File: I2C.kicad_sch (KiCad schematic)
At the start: 16 parts, among them J701 Conn_01x04, J702 Conn_01x04

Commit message: HALMET redesign
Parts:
- removed J701: Conn_01x04, Connector_JST:JST_SH_BM04B-SRSS-TB_1x04-1MP_P1.00mm_Vertical, symbol Connector_Generic:Conn_01x04
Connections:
- net SCL_CONN: now also J702.4 (Pin_4); no longer J702.3 (Pin_3)
- net SDA_CONN: now also J702.3 (Pin_3); no longer J702.4 (Pin_4)
- net +3V3 renamed +3.3V
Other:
- note removed: "I2C (qwiic)"
- title: Sailor Hat with ESP32 -> Hat Labs Marine Engine/Tank interface (HALMET)

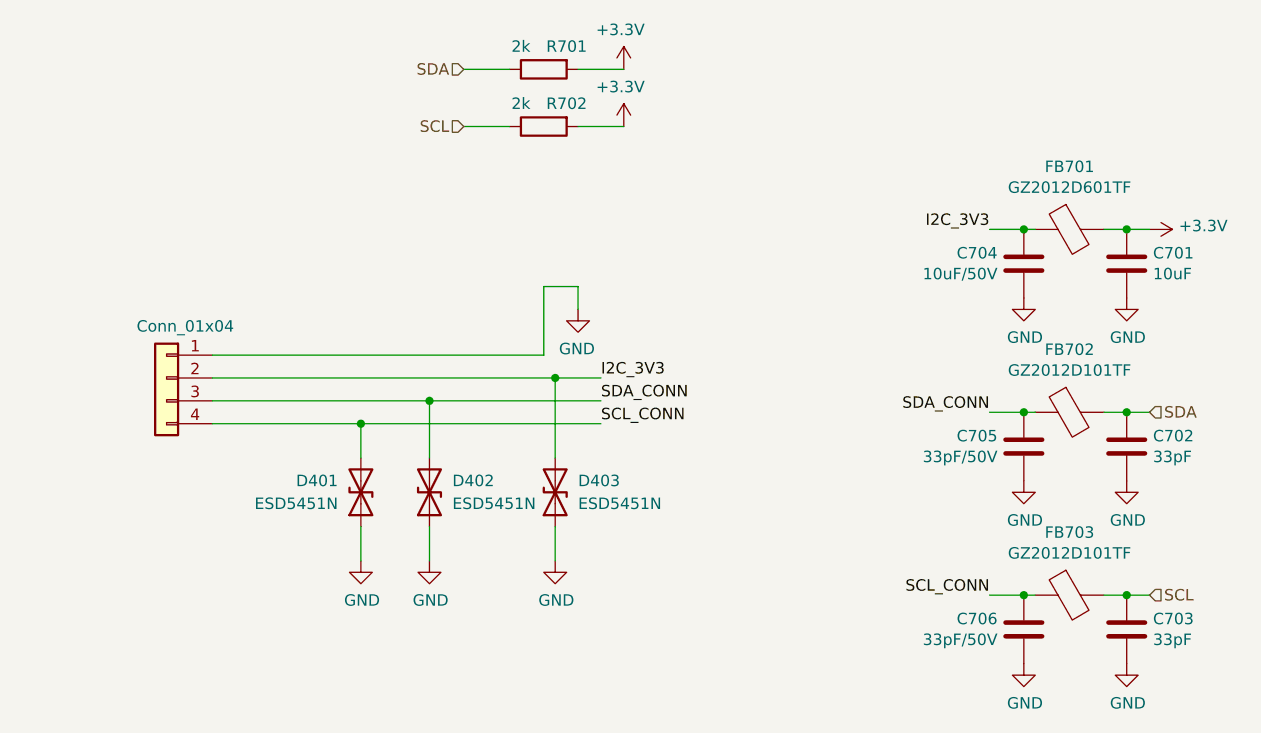
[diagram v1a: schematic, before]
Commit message: Implement HALMET v1.0.0 design changes
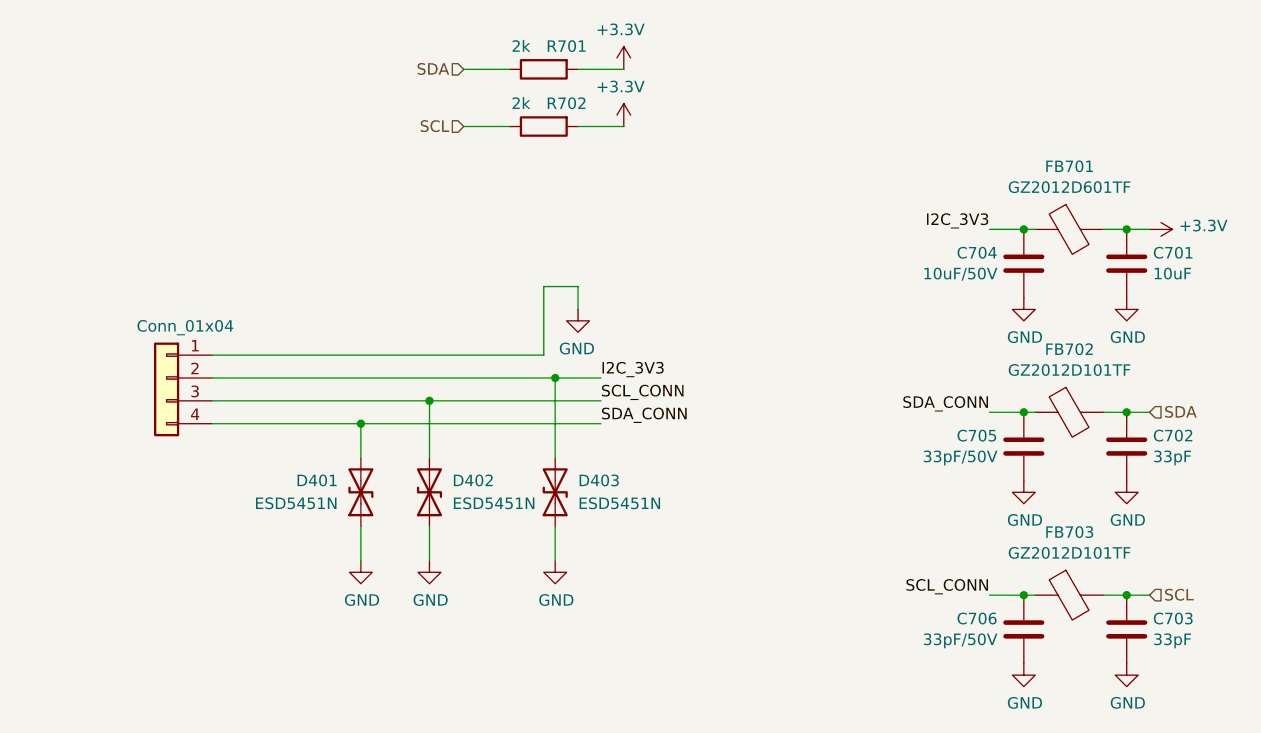
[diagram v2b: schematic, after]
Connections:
- net SCL_CONN: now also D402.2 (A2), J702.3 (Pin_3); no longer D401.2 (A2), J702.4 (Pin_4)
- net SDA_CONN: now also D401.2 (A2), J702.4 (Pin_4); no longer D402.2 (A2), J702.3 (Pin_3)
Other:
- title: Hat Labs Marine Engine/Tank interface (HALMET) -> Hat Labs Marine Engine & Tank interface (HALMET)
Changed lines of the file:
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@@
   (paper "A4")
   (title_block
-    (title "Hat Labs Marine Engine/Tank interface (HALMET)")
-    (date "2023-09-19")
-    (rev "1.0.0-a1")
+    (title "Hat Labs Marine Engine & Tank interface (HALMET)")
+    (date "2023-11-27")
+    (rev "1.0.0")
     (company "Hat Labs Ltd")
     (comment 1 "https://creativecommons.org/licenses/by-sa/4.0")
@@
     (effects (font (size 1.27 1.27)) (justify left bottom))
   )
-  (label "SDA_CONN" (at 90.17 87.63 0) (fields_autoplaced)
+  (label "SDA_CONN" (at 90.17 90.17 0) (fields_autoplaced)
     (effects (font (size 1.27 1.27)) (justify left bottom))
   )
-  (label "SCL_CONN" (at 90.17 90.17 0) (fields_autoplaced)
+  (label "SCL_CONN" (at 90.17 87.63 0) (fields_autoplaced)
     (effects (font (size 1.27 1.27)) (justify left bottom))
   )
